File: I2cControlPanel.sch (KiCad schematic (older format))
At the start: 45 parts, among them J1 Conn_01x08, J2 Conn_01x06, J3 Conn_01x04, J4 Conn_01x04, J5 Conn_01x08, J6 Conn_01x04, SW1 SW_Push, SW2 SW_Push, SW3 SW_Push, SW4 SW_Push, SW5 SlideSwitch, U1 LP2985-3.3, U2 ATmega328PB-MU, U3 AQM0802

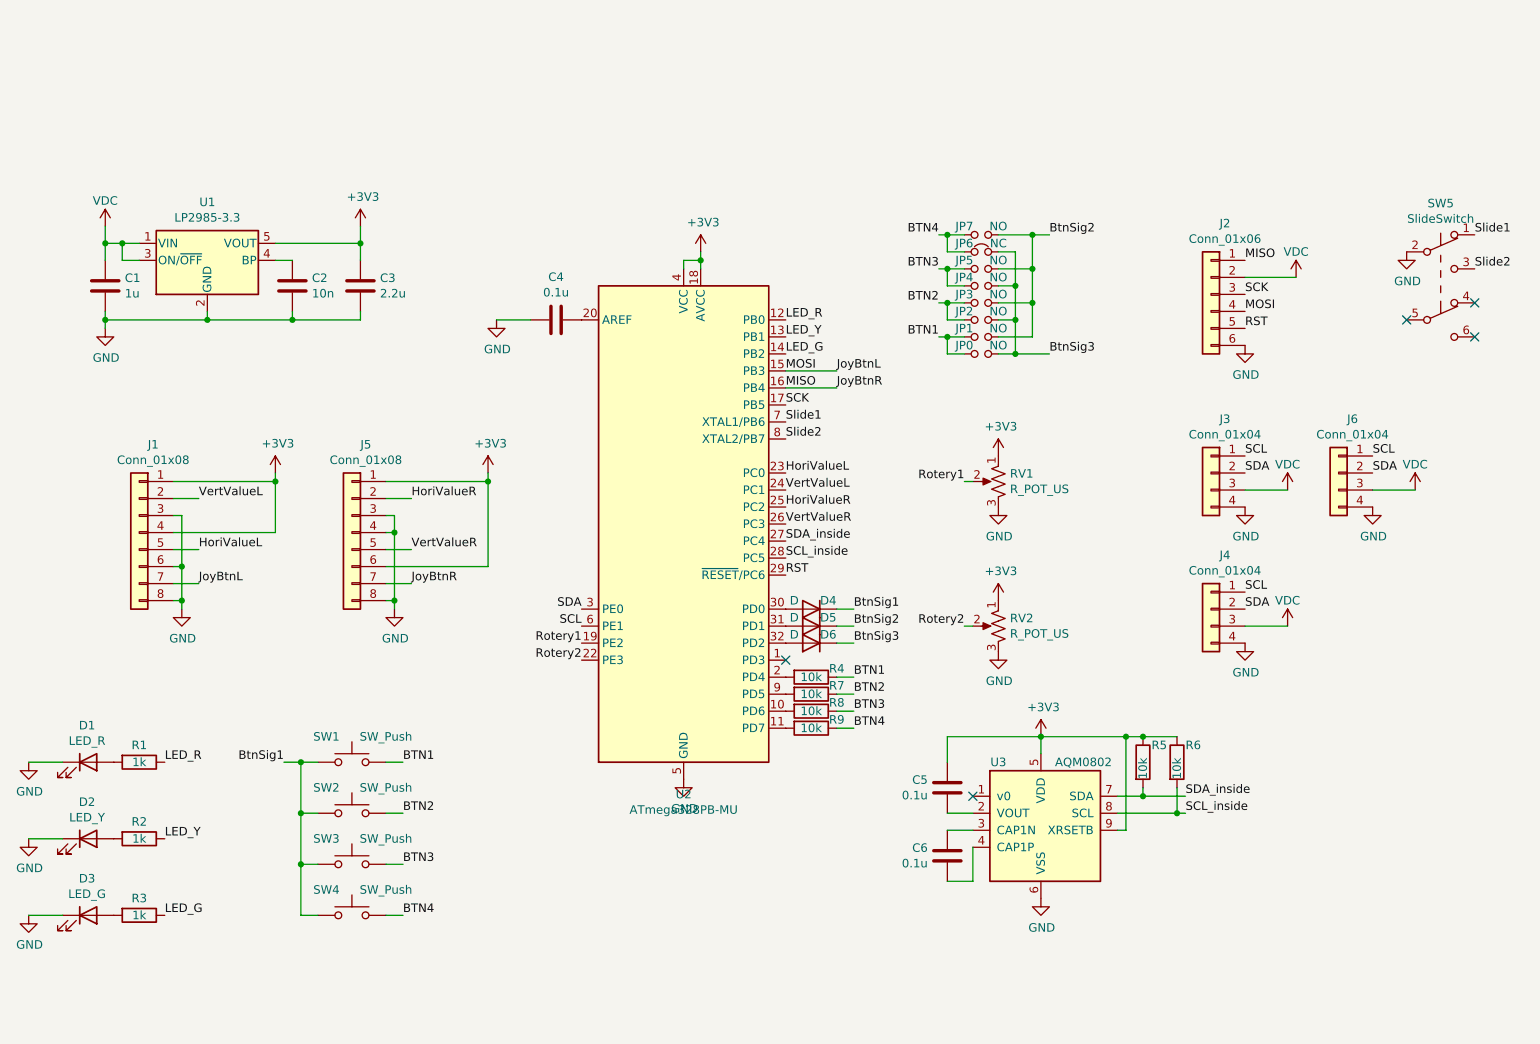
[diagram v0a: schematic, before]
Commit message: Update for rev 2020.08
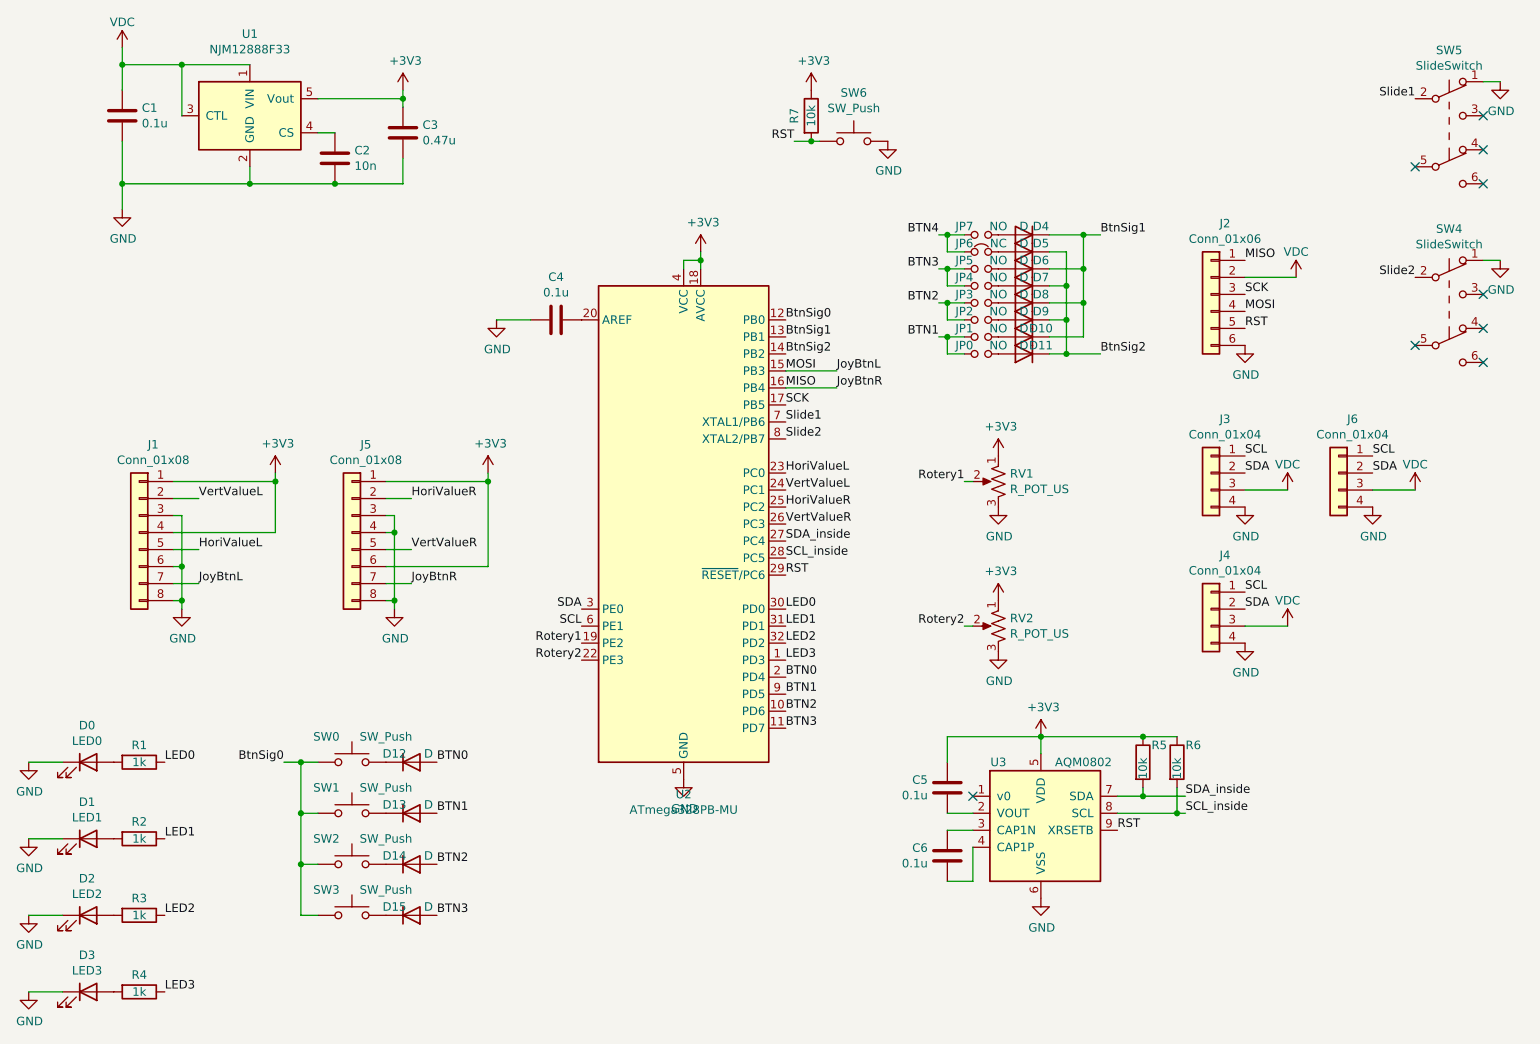
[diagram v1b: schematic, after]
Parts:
- removed R8, R9: 10k, Resistor_SMD:R_0603_1608Metric, symbol Device:R
- removed U1: LP2985-3.3, Package_TO_SOT_SMD:SOT-23-5, symbol Regulator_Linear:LP2985-3.3
- added D10, D11, D12, D13, D14, D15, D7, D8, D9: D, Diode_SMD:D_SOD-323, symbol Device:D
- added D3: LED3, Diode_SMD:D_0603_1608Metric, symbol Device:LED
- added SW4: SlideSwitch, my-kicad-footprints:SlideSwitch, symbol Switch:SW_Push_DPDT
- added SW6: SW_Push, Button_Switch_THT:SW_PUSH_6mm, symbol Switch:SW_Push
- added U1: NJM12888F33, Package_TO_SOT_SMD:SOT-23-5, symbol my-kicad-symbols:NJM12888F33
- C1: value 1u -> 0.1u
- C3: value 2.2u -> 0.47u; footprint Capacitor_SMD:C_0603_1608Metric -> Capacitor_SMD:C_0402_1005Metric
- D0: renamed from D1; value LED_R -> LED0; footprint LED_THT:LED_D5.0mm -> Diode_SMD:D_0603_1608Metric
- D1: renamed from D2; value LED_Y -> LED1; footprint LED_THT:LED_D5.0mm -> Diode_SMD:D_0603_1608Metric
- D2: renamed from D3; value LED_G -> LED2; footprint LED_THT:LED_D5.0mm -> Diode_SMD:D_0603_1608Metric
- D4, D5, D6: footprint Diode_SMD:D_SOD-123 -> Diode_SMD:D_SOD-323
- R4: value 10k -> 1k
- renumbered SW1 to SW0, SW2 to SW1, SW3 to SW2, SW4 to SW3
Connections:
- net +3V3: now also R7.1, U1.5 (Vout); no longer U3.9 (XRSETB)
- net BTN1: now also U2.9 (PD5), D13.2 (A); no longer R4.1, SW0.2
- net BTN2: now also U2.10 (PD6), D14.2 (A); no longer R7.1, SW1.2
- net BTN3: now also U2.11 (PD7), D15.2 (A); no longer SW2.2
- net BTN4: no longer SW3.2
- net BtnSig1: now also D6.1 (K), U2.13 (PB1), D10.1 (K), D8.1 (K); no longer SW0.1, SW1.1, SW2.1, SW3.1
- net BtnSig2: now also U2.14 (PB2), D11.1 (K), D7.1 (K), D9.1 (K); no longer JP1.2, JP3.2, JP5.2, JP7.2
- net GND: now also SW5.1 (A), D3.1 (K), SW4.1 (A), SW6.2, U1.2 (GND); no longer SW5.2 (B)
- net RST: now also R7.2, U3.9 (XRSETB), SW6.1
- net Slide1: now also SW5.2 (B); no longer SW5.1 (A)
- net Slide2: now also SW4.2 (B); no longer SW5.3 (C)
- net VDC: now also U1.1 (VIN), U1.3 (CTL)
- net at C2.1: now also U1.4 (CS)
- net LED3: now reaches U2.1 (PD3)
- net LED3: now also R4.1
- net at R4.2: now also D3.2 (A); no longer U2.2 (PD4)
- net at D4.2 (A): now also JP7.2; no longer U2.30 (PD0)
- net at D5.2 (A): now also JP6.2; no longer U2.31 (PD1)
- net at D6.2 (A): now also JP5.2; no longer U2.32 (PD2)
- removed net BtnSig3: D6.1 (K), JP0.2, JP2.2, JP4.2, JP6.2
- net LED_G renamed LED2
- net LED2: now also U2.32 (PD2); no longer U2.14 (PB2)
- net LED_R renamed BtnSig0
- net BtnSig0: now also SW0.1, SW1.1, SW2.1, SW3.1; no longer R1.1
- net LED_Y renamed LED1
- net LED1: now also U2.31 (PD1); no longer U2.13 (PB1)
- new net: D12.1 (K), SW0.2
- new net: D13.1 (K), SW1.2
- new net: D14.1 (K), SW2.2
- new net: D15.1 (K), SW3.2
- new net: D9.2 (A), JP2.2
- new net: D7.2 (A), JP4.2
- new net: D8.2 (A), JP3.2
- new net: D10.2 (A), JP1.2
- new net: D11.2 (A), JP0.2
- new net BTN0: D12.2 (A), U2.2 (PD4)
- new net LED0: R1.1, U2.30 (PD0)
- no-connect marks 5 -> 9
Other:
- moved on the sheet: C1, C2, C3, D4, SW5

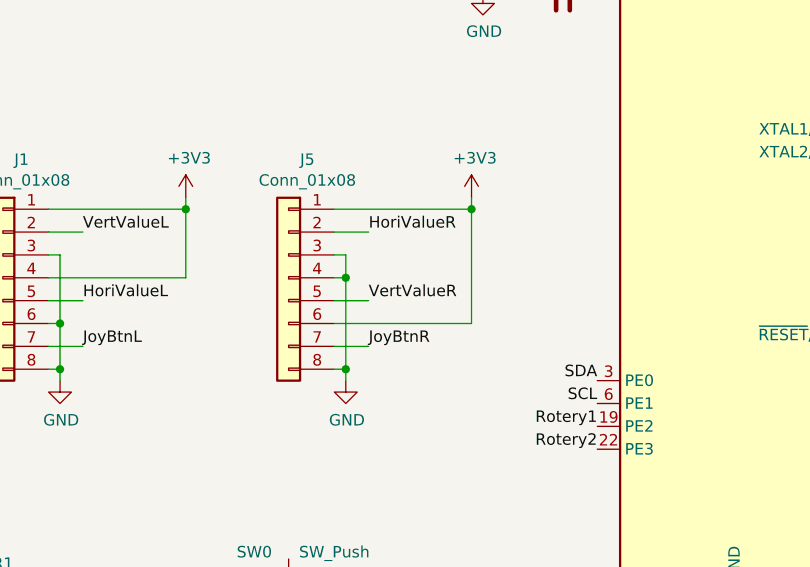
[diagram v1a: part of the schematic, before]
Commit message: Replace gnd and 3v3 for right joy stick
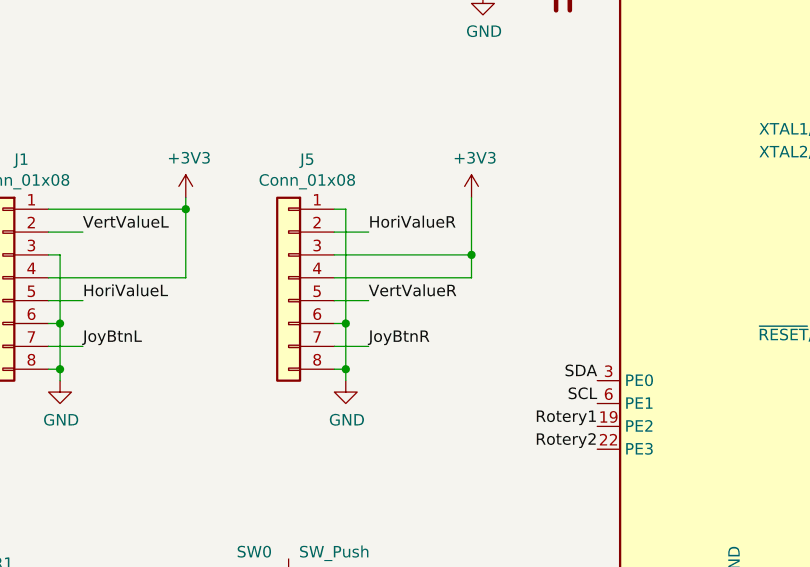
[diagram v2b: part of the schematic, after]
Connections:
- net +3V3: now also J5.3 (Pin_3), J5.4 (Pin_4); no longer J5.1 (Pin_1), J5.6 (Pin_6)
- net GND: now also J5.1 (Pin_1), J5.6 (Pin_6); no longer J5.3 (Pin_3), J5.4 (Pin_4)
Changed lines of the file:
@@
 HoriValueR
 Wire Wire Line
-	4700 3500 4700 3550
-Connection ~ 4700 3550
-Wire Wire Line
 	4250 3650 4100 3650
 Wire Wire Line
 	4100 3950 4250 3950
-Wire Wire Line
-	4100 3550 4700 3550
-Wire Wire Line
-	4100 3750 4150 3750
 $Comp
 L power:GND #PWR0126
@@
 Wire Wire Line
 	4150 4250 4100 4250
-Connection ~ 4150 4250
 Wire Wire Line
 	6750 2900 6450 2900
@@
 Slide2
 NoConn ~ 10550 1800
-Wire Wire Line
-	4150 3750 4150 3850
-Wire Wire Line
-	4700 4050 4100 4050
-Wire Wire Line
-	4700 3550 4700 4050
-Wire Wire Line
-	4100 3850 4150 3850
-Connection ~ 4150 3850
-Wire Wire Line
-	4150 3850 4150 4250
 Text Label 6450 4600 0    50   ~ 0
 LED3
@@
 Wire Wire Line
 	10550 2250 10650 2250
+Wire Wire Line
+	4100 3850 4700 3850
+Wire Wire Line
+	4100 3750 4700 3750
+Connection ~ 4700 3750
+Wire Wire Line
+	4700 3750 4700 3850
+Wire Wire Line
+	4700 3500 4700 3750
+Wire Wire Line
+	4100 3550 4150 3550
+Wire Wire Line
+	4150 3550 4150 4050
+Connection ~ 4150 4250
+Wire Wire Line
+	4150 4050 4100 4050
+Connection ~ 4150 4050
+Wire Wire Line
+	4150 4050 4150 4250
 $EndSCHEMATC

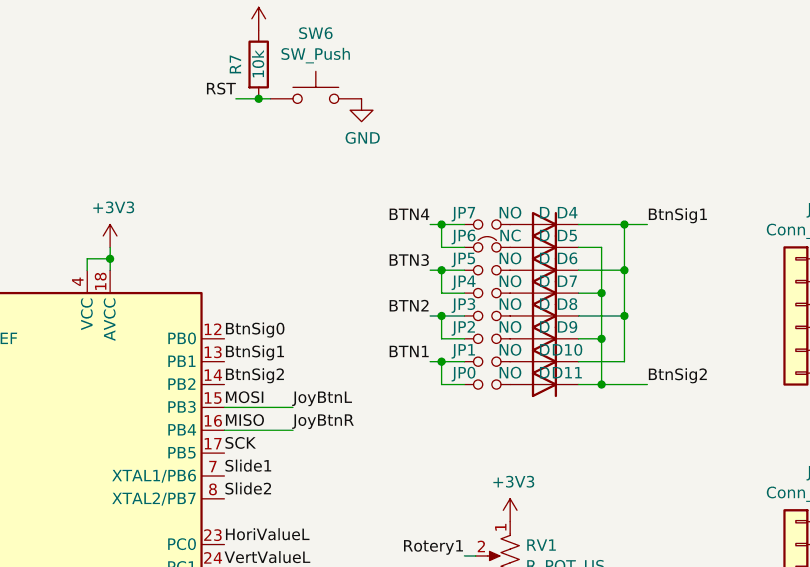
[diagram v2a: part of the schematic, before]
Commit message: Correct button line for address pads
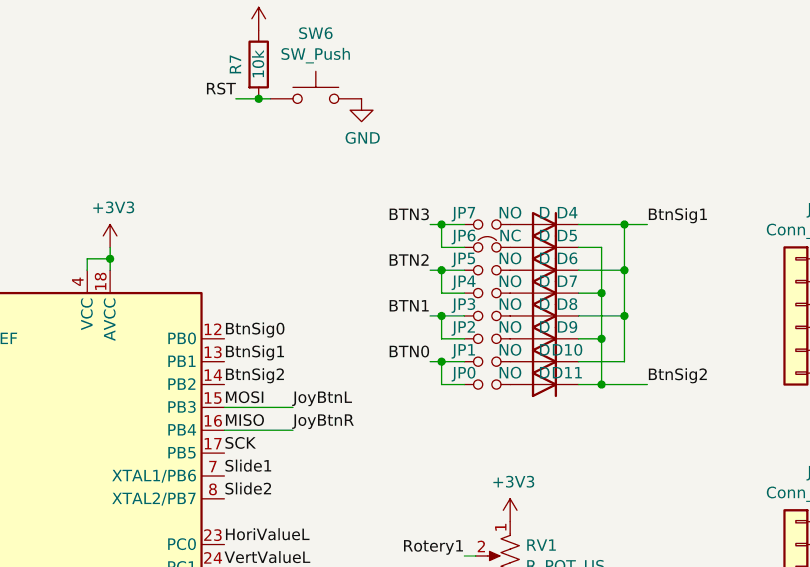
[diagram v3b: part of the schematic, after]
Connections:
- net BTN4 is gone; now on net BTN3: JP6.1, JP7.1
- net BTN0: now also JP0.1, JP1.1
- net BTN1: now also JP2.1, JP3.1; no longer JP0.1, JP1.1
- net BTN2: now also JP4.1, JP5.1; no longer JP2.1, JP3.1
- net BTN3: no longer JP4.1, JP5.1
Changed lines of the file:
@@
 $EndComp
 Text Label 7350 2700 2    50   ~ 0
+BTN0
+Text Label 7350 2500 2    50   ~ 0
 BTN1
-Text Label 7350 2500 2    50   ~ 0
+Text Label 7350 2300 2    50   ~ 0
 BTN2
-Text Label 7350 2300 2    50   ~ 0
+Text Label 7350 2100 2    50   ~ 0
 BTN3
-Text Label 7350 2100 2    50   ~ 0
-BTN4
 Wire Wire Line
 	7350 2500 7400 2500
